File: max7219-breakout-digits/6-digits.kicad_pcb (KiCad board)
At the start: 2 copper layers, 66 x 12 mm, 6 parts, among them J1 Conn_02x08_Odd_Even, U1 7Segment 3 digit CC_STH, U2 7Segment 3 digit CC_STH

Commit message: MF Logo on correct positions, wrong link deleted
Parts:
- moved G2 2.97 mm to (112.5, 64.0)
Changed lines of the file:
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@@
 	(title_block
 		(title "7 Segment Display Module, 6 digits")
-		(date "2025-11")
-		(rev "V5.2")
+		(date "2025-12")
+		(rev "V6.0")
 		(company "MobiFlight")
 	)
@@
 	(footprint "MobiFlight:MobiFlight-Logo-Small"
 		(layer "B.Cu")
-		(at 114.09 61.43 180)
+		(at 112.52 63.95 180)
 		(property "Reference" "G2"
 			(at 0 0 0)

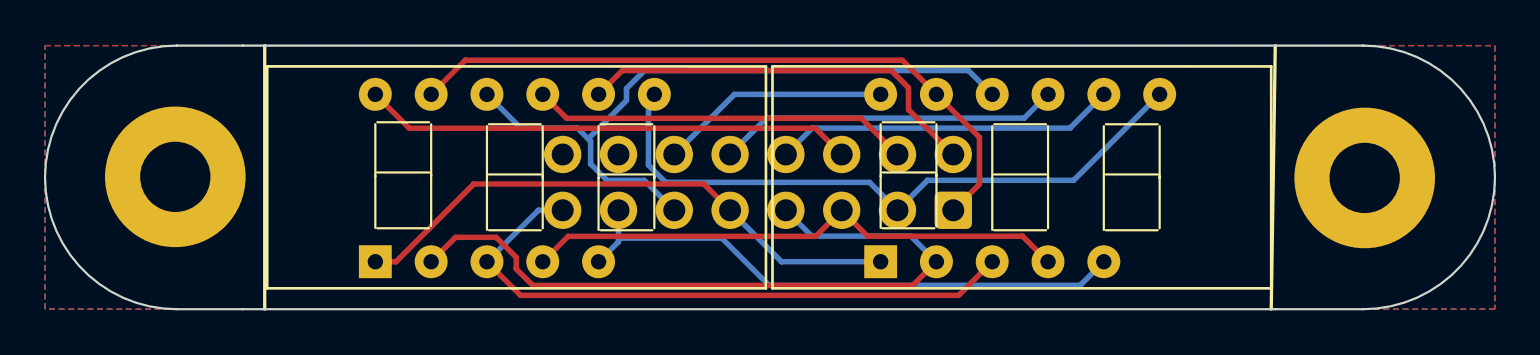
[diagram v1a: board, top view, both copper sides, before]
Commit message: slight movement of mounting holes to get full millimeters
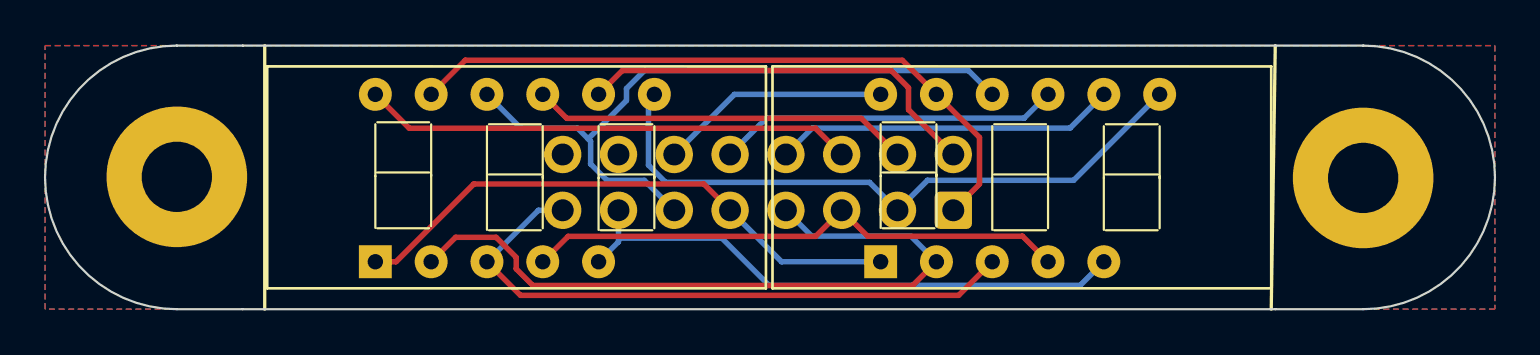
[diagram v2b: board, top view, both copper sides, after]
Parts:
- moved H2 0.07 mm to (119.0, 62.6)
- moved H1 0.07 mm to (65.0, 62.5)
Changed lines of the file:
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@@
 	(footprint "MountingHole:MountingHole_3.2mm_M3_Pad"
 		(layer "F.Cu")
-		(at 64.8866 62.5303)
+		(at 64.9566 62.5303)
 		(descr "Mounting Hole 3.2mm, M3, generated by kicad-footprint-generator mountinghole.py")
 		(tags "mountinghole M3")
@@
 	(footprint "MountingHole:MountingHole_3.2mm_M3_Pad"
 		(layer "F.Cu")
-		(at 119.0266 62.5803)
+		(at 118.9566 62.5803)
 		(descr "Mounting Hole 3.2mm, M3, generated by kicad-footprint-generator mountinghole.py")
 		(tags "mountinghole M3")
@@
 	)
 	(group ""
-		(members "30c89fb0-d144-491c-8651-f7c9b18de9aa" "41b2a191-795c-4d2e-aa3b-11d277b062b3")
-	)
-	(group ""
